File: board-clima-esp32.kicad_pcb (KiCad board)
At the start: 2 copper layers, 96.5 x 96.5 mm, 29 parts, among them IC1 ESP32-S3-WROOM-1-N8, J2 Screw_Terminal_01x03, J3 Conn_01x04_Pin, J4 Conn_01x04_Pin, J5 Conn_01x03_Pin, J6 USB_C_Receptacle, Q1 2N7002K, SW1 RESET, SW2 BOOT, U1 AMS1117-3.3, U2 JZC-32F/C

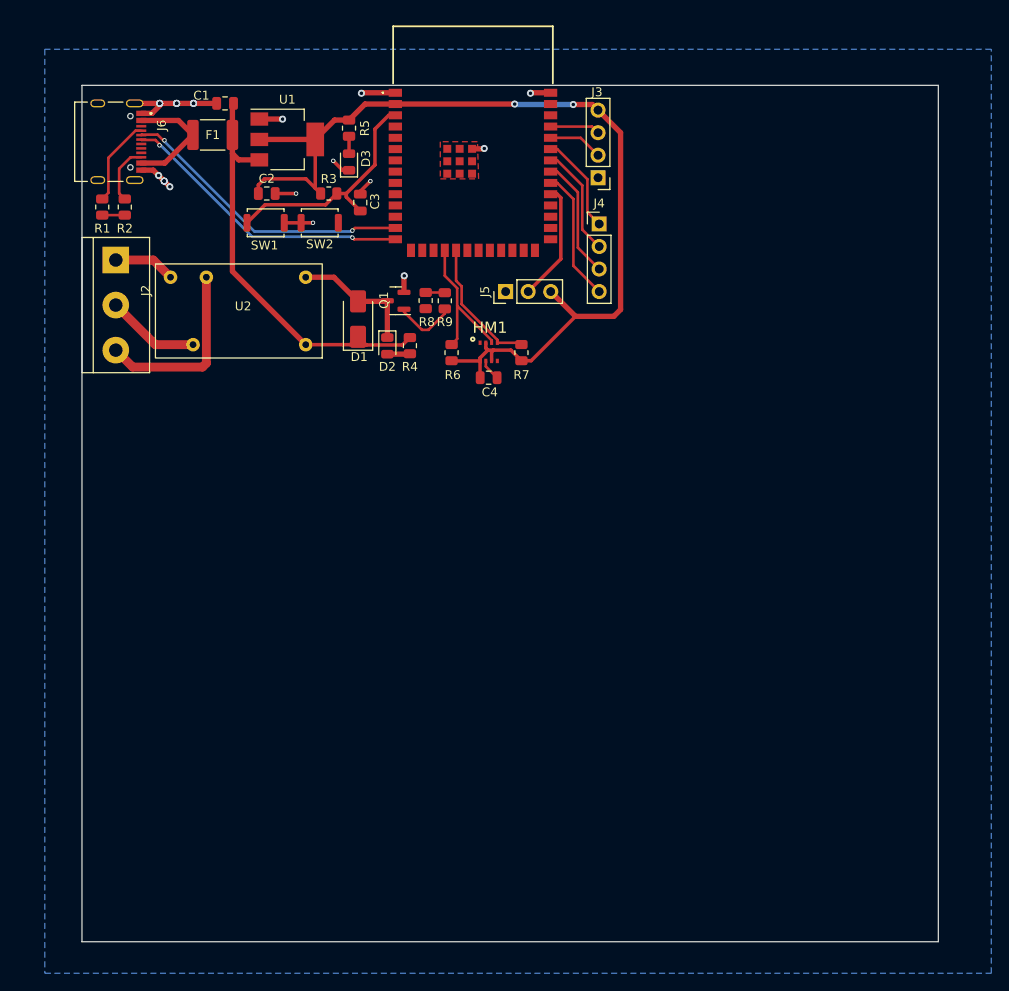
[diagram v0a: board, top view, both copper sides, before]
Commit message: usb pads, via sizes
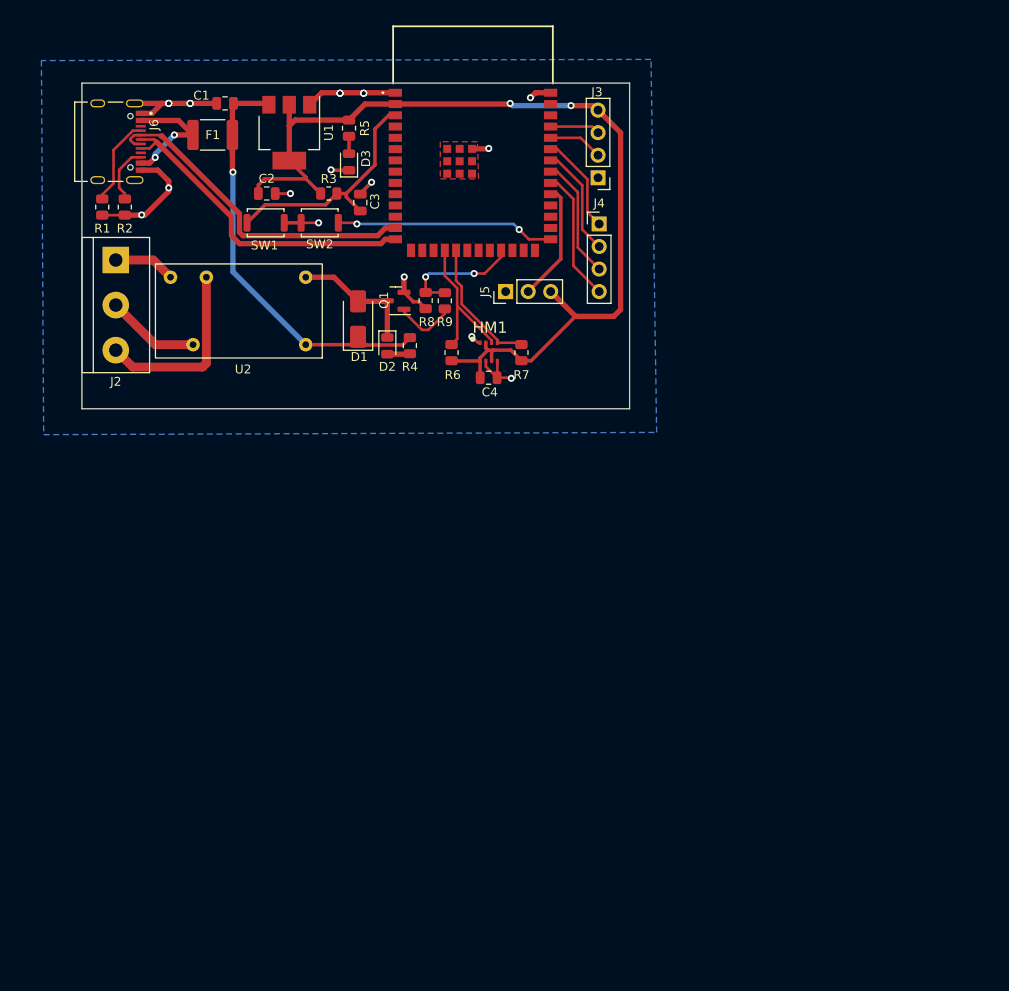
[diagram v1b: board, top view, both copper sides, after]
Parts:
- moved U1 0.80 mm to (116.5, 60.2), turned to -90 degrees
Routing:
- net /BOOT: track 0.00 -> 24.7 mm, vias 0 -> 2
- net GND: track 42.8 -> 61.8 mm
- net /RELAY: track 2.17 -> 14.1 mm, vias 0 -> 2
- net /USB-: track 33.4 -> 37.7 mm, vias 2 -> 0
- net /USB+: track 33.4 -> 37.3 mm, vias 2 -> 0
- net +5V: track 46.8 -> 47.7 mm, vias 0 -> 1
- net Net-(F1-Pad1): track 13.6 -> 14.0 mm, vias 0 -> 2
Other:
- board size 96.5 x 96.5 mm -> 61.7 x 36.7 mm

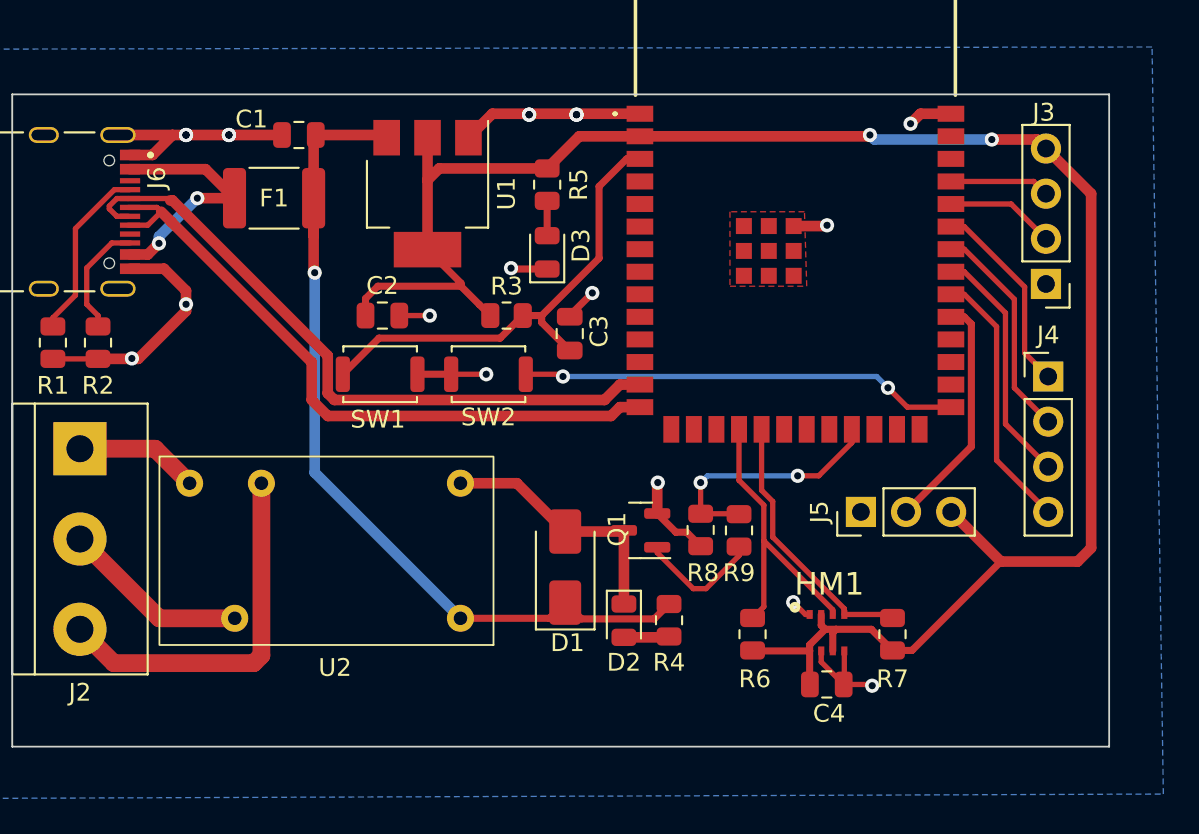
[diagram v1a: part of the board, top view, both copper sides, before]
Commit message: moved bme280
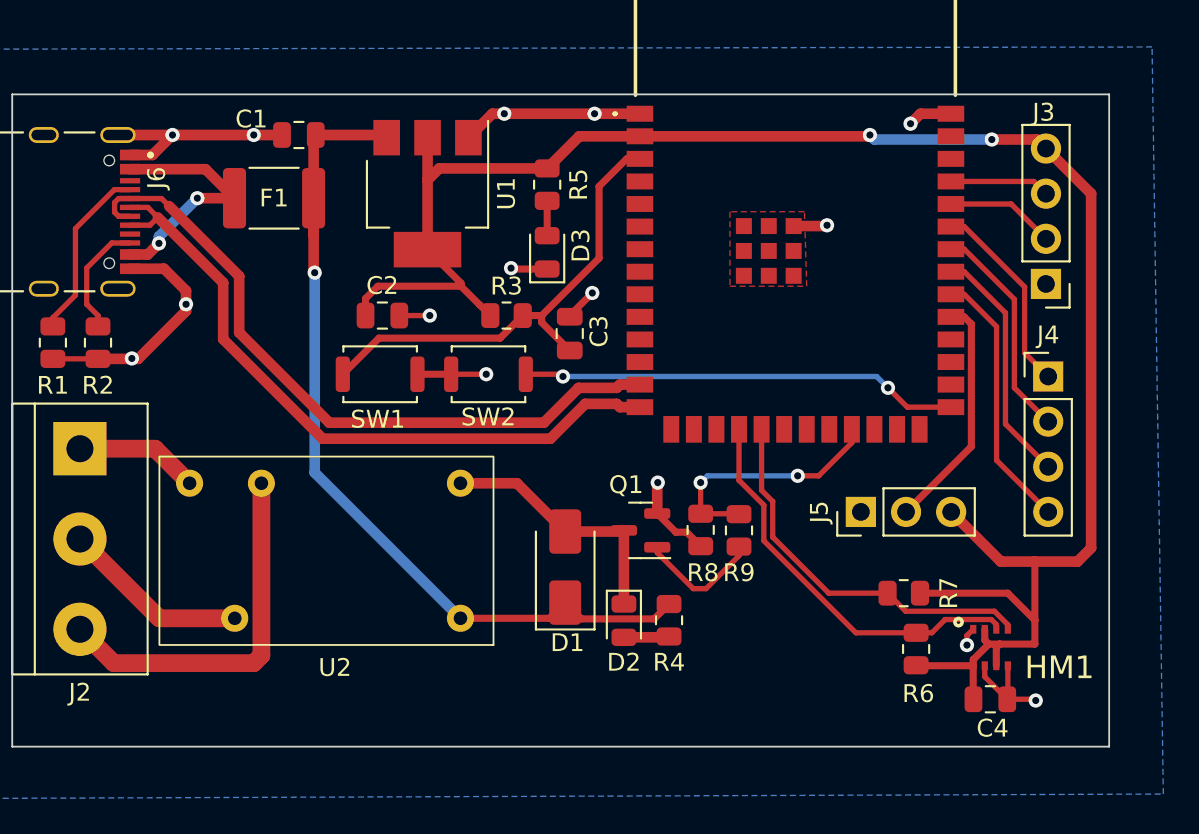
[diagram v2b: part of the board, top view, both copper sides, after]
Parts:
- moved HM1 9.24 mm to (147.2, 86.8)
- moved C4 9.24 mm to (148.1, 88.6)
- moved R6 9.24 mm to (144.0, 85.8)
- moved R7 2.40 mm to (143.3, 82.7), turned to 180 degrees
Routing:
- net /SCK: track 15.1 -> 21.9 mm
- net /SDA: track 17.2 -> 22.8 mm
- net +3.3V: track 108.5 -> 110.4 mm
- net /USB-: track 37.7 -> 39.1 mm
- net /USB+: track 37.3 -> 38.6 mm
- net GND: track 61.8 -> 61.6 mm, vias 19 -> 15

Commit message: should be done
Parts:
- J3 UART: renamed from J3
- J4 JTAG: renamed from J4
- moved D3 17.7 mm to (106.9, 56.5), turned to 0 degrees
- moved R6 13.5 mm to (132.2, 79.2)
- moved C1 13.3 mm to (121.3, 62.5), turned to -90 degrees
- moved R5 12.9 mm to (110.7, 56.5), turned to 180 degrees
- moved C2 12.7 mm to (122.0, 57.3), turned to 180 degrees
- moved R1 12.2 mm to (103.7, 59.6), turned to 0 degrees
- moved SW1 10.1 mm to (123.1, 66.4), turned to 0 degrees
- moved R3 7.84 mm to (123.0, 59.5)
- moved R7 7.11 mm to (137.0, 79.3), turned to 90 degrees
- moved R2 6.00 mm to (102.8, 65.1)
- moved C3 5.62 mm to (123.7, 62.5), turned to -90 degrees
- moved SW2 5.48 mm to (116.1, 66.4), turned to 0 degrees
- moved Q1 5.38 mm to (124.4, 75.6)
- moved D2 5.03 mm to (127.4, 79.2)
- moved R8 4.47 mm to (129.8, 83.1)
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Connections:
- IC1 pad 16: unconnected-(IC1-IO46-Pad16) -> /RELAY
- IC1 pad 23: /RELAY -> unconnected-(IC1-IO21-Pad23)
- J6 pad S2: (no net) -> GND
- J6 pad S3: (no net) -> GND
- J6 pad S4: (no net) -> GND
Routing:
- net GND: track 61.6 -> 36.2 mm, vias 15 -> 27
- net Net-(IC1-EN): track 26.7 -> 14.7 mm
- net /BOOT: track 24.7 -> 34.2 mm
- net Net-(J6-CC1): track 10.0 -> 3.17 mm
- net /SDA: track 22.8 -> 29.3 mm
- net /RELAY: track 14.1 -> 9.58 mm, vias 2 -> 0
- net /SCK: track 21.9 -> 26.2 mm
- net /USB+: track 38.6 -> 35.1 mm
- net +5V: track 47.7 -> 50.8 mm, vias 1 -> 3
- net Net-(J2-Pin_3): track 20.9 -> 23.6 mm
- net /USB-: track 39.1 -> 36.8 mm
- net +3.3V: track 110.4 -> 112.5 mm, vias 2 -> 3
- net Net-(J6-CC2): track 6.57 -> 4.68 mm
- net Net-(Q1-G): track 7.02 -> 5.18 mm
- net Net-(F1-Pad1): track 14.0 -> 15.5 mm
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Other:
- board size 61.7 x 36.7 mm -> 63.4 x 38.5 mm
- board text added: "3V3"
- board text added: "EDOARDO FULLIN REV1 202310 NO WARRANTY WHATSOEVER"
- board text added: "GND"
- board text added: "IO38"
- board text added: "RX"
- board text added: "TCK"
- board text added: "TDI"
- board text added: "TDO"
- board text added: "TMS"
- board text added: "TX"

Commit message: editing stuff again
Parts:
- removed J4 JTAG: Conn_01x04_Pin, Connector_PinHeader_2.54mm:PinHeader_1x04_P2.54mm_Vertical
- added H1: MountingHole, MountingHole:MountingHole_2.5mm, F.Cu at (106.6, 71.8)
- added H2: MountingHole, MountingHole:MountingHole_2.5mm, F.Cu at (141.0, 78.5)
- added J1: Conn_01x02_Pin, Connector_PinHeader_2.54mm:PinHeader_1x02_P2.54mm_Vertical, F.Cu at (136.1, 90.3)
- added J4: Conn_01x04_Pin, Connector_PinHeader_1.00mm:PinHeader_1x05_P1.00mm_Vertical, F.Cu at (149.6, 79.1)
- J3: renamed from J3 UART
- J5: value Conn_01x03_Pin -> Conn_01x04_Pin; footprint Connector_PinHeader_2.54mm:PinHeader_1x03_P2.54mm_Vertical -> Connector_PinHeader_2.54mm:PinHeader_1x04_P2.54mm_Vertical
- moved J5 17.6 mm to (151.1, 63.9), turned to 180 degrees
- moved J3 10.7 mm to (151.1, 75.9)
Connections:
- IC1 pad 31: /GPIO38 -> unconnected-(IC1-IO38-Pad31)
- IC1 pad 38: unconnected-(IC1-IO2-Pad38) -> /GPIO2
- IC1 pad 39: unconnected-(IC1-IO1-Pad39) -> /GPIO1
- J5 pad 2: /GPIO38 -> /GPIO2
- J5 pad 3: +3.3V -> /GPIO1
- J6 pad S2: GND -> (no net)
- J6 pad S3: GND -> (no net)
- J6 pad S4: GND -> (no net)
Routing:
- net /GPIO38: track 13.4 -> 0.00 mm
- net /JTAG_TMS: track 11.1 -> 22.3 mm
- net /JTAG_TDI: track 12.4 -> 23.1 mm, vias 0 -> 2
- net /UART_RX: track 6.16 -> 15.2 mm
- net /UART_TX: track 5.63 -> 13.9 mm
- net /GPIO2: track 0.00 -> 6.52 mm
- net /JTAG_TDO: track 13.7 -> 20.1 mm, vias 0 -> 2
- net /GPIO1: track 0.00 -> 5.98 mm
- net /SCK: track 26.2 -> 31.0 mm
- net /SDA: track 29.3 -> 33.5 mm, vias 0 -> 2
- net /JTAG_TCK: track 15.0 -> 17.8 mm
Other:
- outline, holes or cut-outs redrawn
- board text added: "EDOARDO FULLIN REV1 202310 NO WARRANTY WHATSOEVER USAGE AT USER'S OWN RISK"
- board text added: "GPIO"
- board text added: "I2C"
- board text added: "I2C PUN"
- board text added: "IO1"
- board text added: "IO2"
- board text added: "JTAG"
- board text added: "SCK"
- board text added: "SDA"
- board text added: "UART"
- board text removed: "EDOARDO FULLIN REV1 202310 NO WARRANTY WHATSOEVER"
- board text removed: "IO38"
- board text removed: "TCK"
- board text removed: "TDI"
- board text removed: "TDO"
- board text removed: "TMS"

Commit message: edit to get jlc assembly
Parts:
- D1: value MRA4007T3G -> SM4007; footprint Diode_SMD:D_SMA -> Diode_SMD:D_MELF
- J1: footprint Connector_PinHeader_2.54mm:PinHeader_1x02_P2.54mm_Vertical -> Connector_PinHeader_2.54mm:PinHeader_1x03_P2.54mm_Vertical
- Q1: value 2N7002K -> AO3400A
- SW1, SW2: footprint Button_Switch_SMD:SW_Push_SPST_NO_Alps_SKRK -> Button_Switch_SMD:SW_Push_1P1T_XKB_TS-1187A
- moved J1 2.79 mm to (133.3, 90.3)
- moved SW2 1.52 mm to (114.9, 67.3), turned to 180 degrees
- moved SW1 1.13 mm to (122.4, 67.3), turned to 180 degrees
- moved Q1 0.67 mm to (124.4, 74.9), turned to 0 degrees
- moved D1 0.45 mm to (124.1, 80.8)
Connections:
- J1 pad 1: /SCK -> GND
- J1 pad 2: /SDA -> /SCK
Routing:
- net Net-(IC1-EN): track 14.7 -> 19.5 mm
- net GND: track 36.2 -> 32.2 mm, vias 27 -> 26
- net Net-(Q1-G): track 5.18 -> 8.32 mm
- net +5V: track 50.8 -> 48.0 mm
- net /BOOT: track 34.2 -> 35.3 mm
- net Net-(D1-A): track 13.0 -> 13.9 mm
- net /SDA: track 33.5 -> 34.0 mm
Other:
- board text added: "BOOT"
- board text added: "JLCJLCJLCJLC"
- board text added: "RESET"

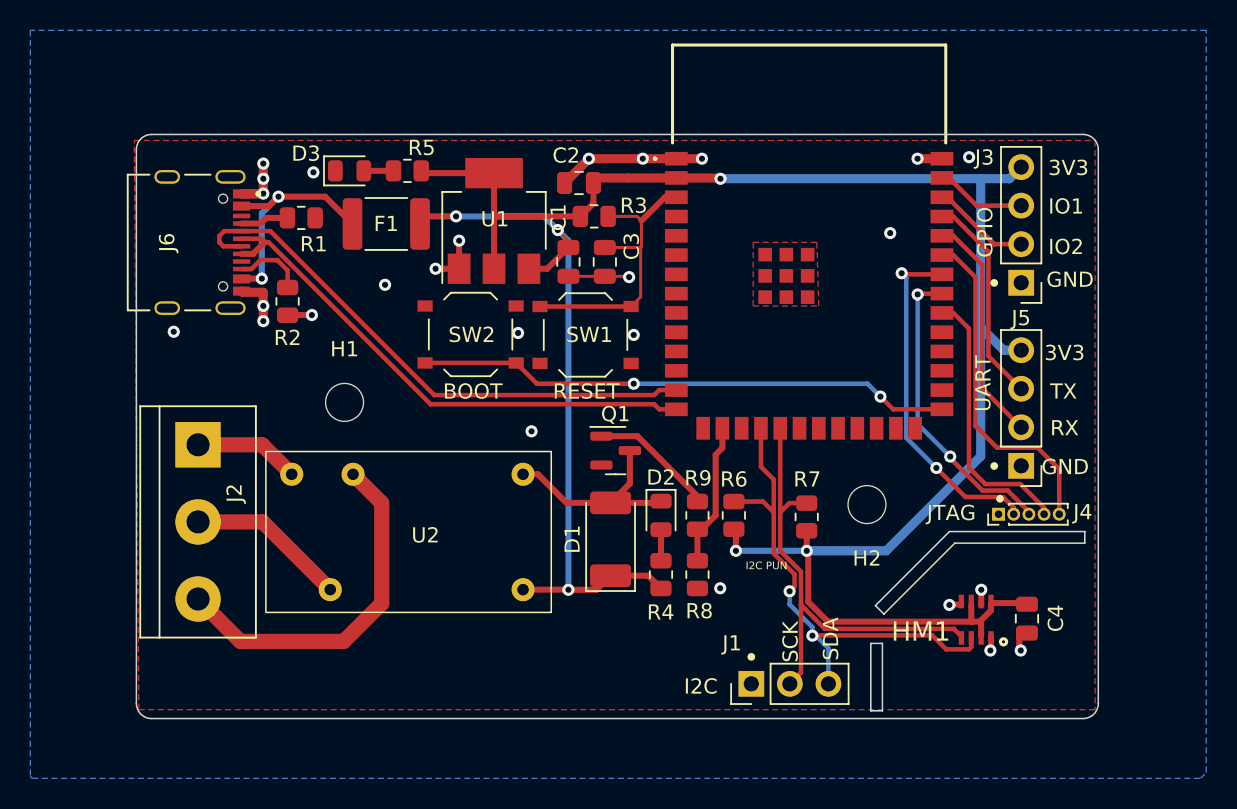
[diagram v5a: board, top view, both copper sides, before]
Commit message: component edits, terminalblock footprint
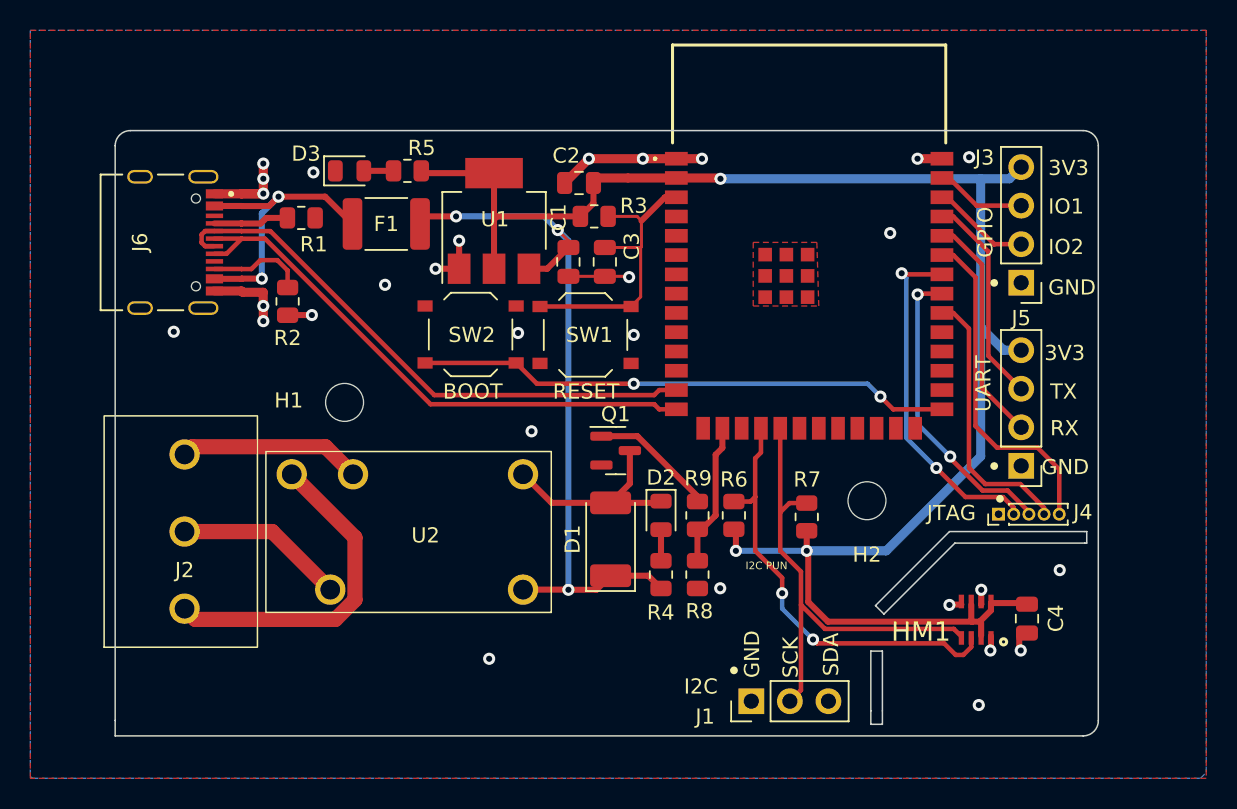
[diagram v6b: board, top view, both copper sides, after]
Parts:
- IC1: value ESP32-S3-WROOM-1-N8 -> ESP32-S3-WROOM-1-N4
- J2: footprint TerminalBlock:TerminalBlock_bornier-3_P5.08mm -> XYEK500-5.08-3P:XYEK500-5.08-3P
- moved J2 14.7 mm to (90.7, 87.9), turned to 90 degrees
- moved J6 1.79 mm to (93.1, 61.2)
- moved J1 1.14 mm to (133.3, 91.4)
- moved H2 0.25 mm to (141.0, 78.2)
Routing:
- net Net-(J2-Pin_1): track 6.97 -> 22.1 mm
- net Net-(J2-Pin_3): track 23.6 -> 12.1 mm
- net /SDA: track 34.0 -> 29.2 mm
- net GND: track 32.2 -> 35.8 mm, vias 26 -> 29
- net Net-(F1-Pad1): track 15.5 -> 19.1 mm
- net /USB+: track 35.1 -> 37.3 mm
- net Net-(J6-CC2): track 4.68 -> 6.48 mm
- net Net-(J6-CC1): track 3.17 -> 4.96 mm
- net /SCK: track 31.1 -> 32.3 mm
- net Net-(J2-Pin_2): track 10.6 -> 11.2 mm
- net /USB-: track 36.8 -> 37.5 mm
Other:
- board size 63.4 x 38.5 mm -> 64.8 x 39.9 mm
- board text added: "${COMMENT1}"
- board text added: "${COMPANY} ${REVISION} NO WARRANTY WHATSOEVER USAGE AT USER'S OWN RISK"
- board text removed: "EDOARDO FULLIN REV1 202310 NO WARRANTY WHATSOEVER USAGE AT USER'S OWN RISK"

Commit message: was about to fuck everything up
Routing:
- net /SDA: track 29.2 -> 33.7 mm
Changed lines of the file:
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@@
   (segment (start 133.604 81.534) (end 133.604 77.978) (width 0.3) (layer "F.Cu") (net 9))
   (segment (start 135.382 83.312) (end 133.604 81.534) (width 0.3) (layer "F.Cu") (net 9))
+  (segment (start 137.414 90.424) (end 138.43 91.44) (width 0.3) (layer "F.Cu") (net 9))
   (segment (start 146.05 87.63) (end 138.684 87.63) (width 0.3) (layer "F.Cu") (net 9))
   (segment (start 133.604 75.438) (end 133.985 75.057) (width 0.3) (layer "F.Cu") (net 9))
@@
   (segment (start 133.604 77.978) (end 133.2945 78.2875) (width 0.3) (layer "F.Cu") (net 9))
   (segment (start 147.840055 87.274055) (end 147.840055 87.871945) (width 0.3) (layer "F.Cu") (net 9))
+  (segment (start 137.414 87.376) (end 137.414 90.424) (width 0.3) (layer "F.Cu") (net 9))
   (via (at 137.414 87.376) (size 0.8) (drill 0.4) (layers "F.Cu" "B.Cu") (net 9))
   (via (at 135.382 84.328) (size 0.8) (drill 0.4) (layers "F.Cu" "B.Cu") (net 9))

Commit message: cleanup and some helper in schematic
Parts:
- J4: footprint Connector_PinHeader_1.00mm:PinHeader_1x05_P1.00mm_Vertical -> Connector_PinHeader_2.54mm:PinHeader_1x05_P2.54mm_Vertical
- moved D3 16.9 mm to (123.8, 57.5), turned to 90 degrees
- moved H2 15.3 mm to (151.8, 89.0)
- moved J4 12.3 mm to (137.4, 77.5)
- moved R5 10.8 mm to (121.4, 57.5), turned to 90 degrees
- moved J1 8.89 mm to (137.9, 83.8), turned to -90 degrees
- moved C4 5.87 mm to (145.8, 84.8), turned to 0 degrees
- moved F1 5.54 mm to (105.0, 56.5)
- moved C1 5.50 mm to (119.0, 57.5), turned to 90 degrees
- moved C2 5.16 mm to (119.0, 61.5), turned to -90 degrees
- moved HM1 4.90 mm to (145.9, 88.7), turned to 180 degrees
- moved U1 3.41 mm to (113.0, 59.5), turned to 180 degrees
- moved R7 2.81 mm to (134.2, 79.1)
- moved J3 2.80 mm to (153.4, 77.5)
- moved J5 2.76 mm to (153.4, 65.4)
- moved H1 2.70 mm to (104.5, 70.0)
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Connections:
- J6 pad S1: GND -> unconnected-(J6-SHIELD-PadS1)
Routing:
- net GND: track 35.8 -> 46.3 mm, vias 29 -> 51
- net /SCK: track 32.3 -> 22.5 mm
- net /SDA: track 33.7 -> 25.1 mm, vias 2 -> 0
- net Net-(F1-Pad1): track 19.1 -> 13.3 mm
- net /JTAG_TDI: track 23.1 -> 17.9 mm, vias 2 -> 1
- net /JTAG_TMS: track 22.3 -> 17.3 mm
- net /JTAG_TDO: track 20.1 -> 15.5 mm, vias 2 -> 1
- net /BOOT: track 35.3 -> 39.8 mm
- net /UART_TX: track 13.9 -> 17.6 mm
- net /UART_RX: track 15.2 -> 18.8 mm
- net /GPIO2: track 6.52 -> 9.88 mm
- net /GPIO1: track 5.98 -> 8.91 mm
- net Net-(J2-Pin_1): track 22.1 -> 24.8 mm
- net /JTAG_TCK: track 17.8 -> 15.4 mm, vias 0 -> 1
- net +5V: track 48.0 -> 50.4 mm, vias 3 -> 1
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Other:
- outline, holes or cut-outs redrawn
- board text removed: "I2C PUN"
- board text removed: "JLCJLCJLCJLC"
